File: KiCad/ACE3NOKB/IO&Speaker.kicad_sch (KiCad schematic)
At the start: 24 parts, among them Q3 BC183

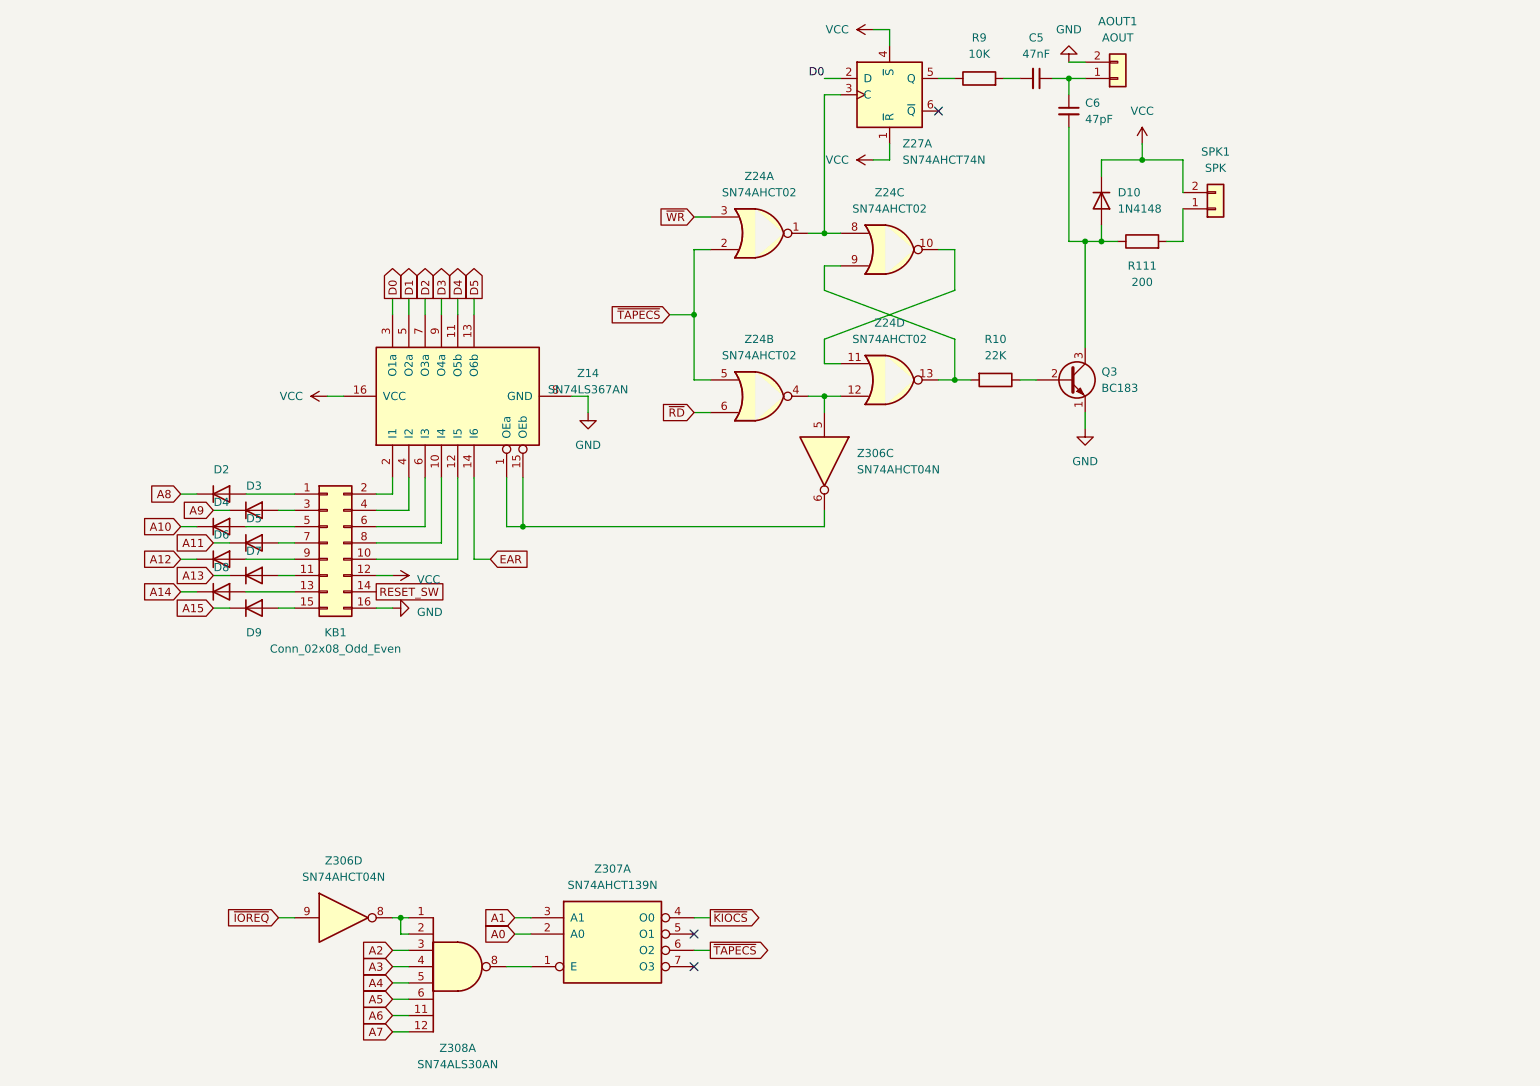
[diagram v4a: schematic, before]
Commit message: Some surface mounted devices and 1G gates for space. Switch able bwteen speeds and witha Freuqency Multiplier to augment the orginal crystal.
Signed-off-by: John Bradley <flypie@rocketmail.com>
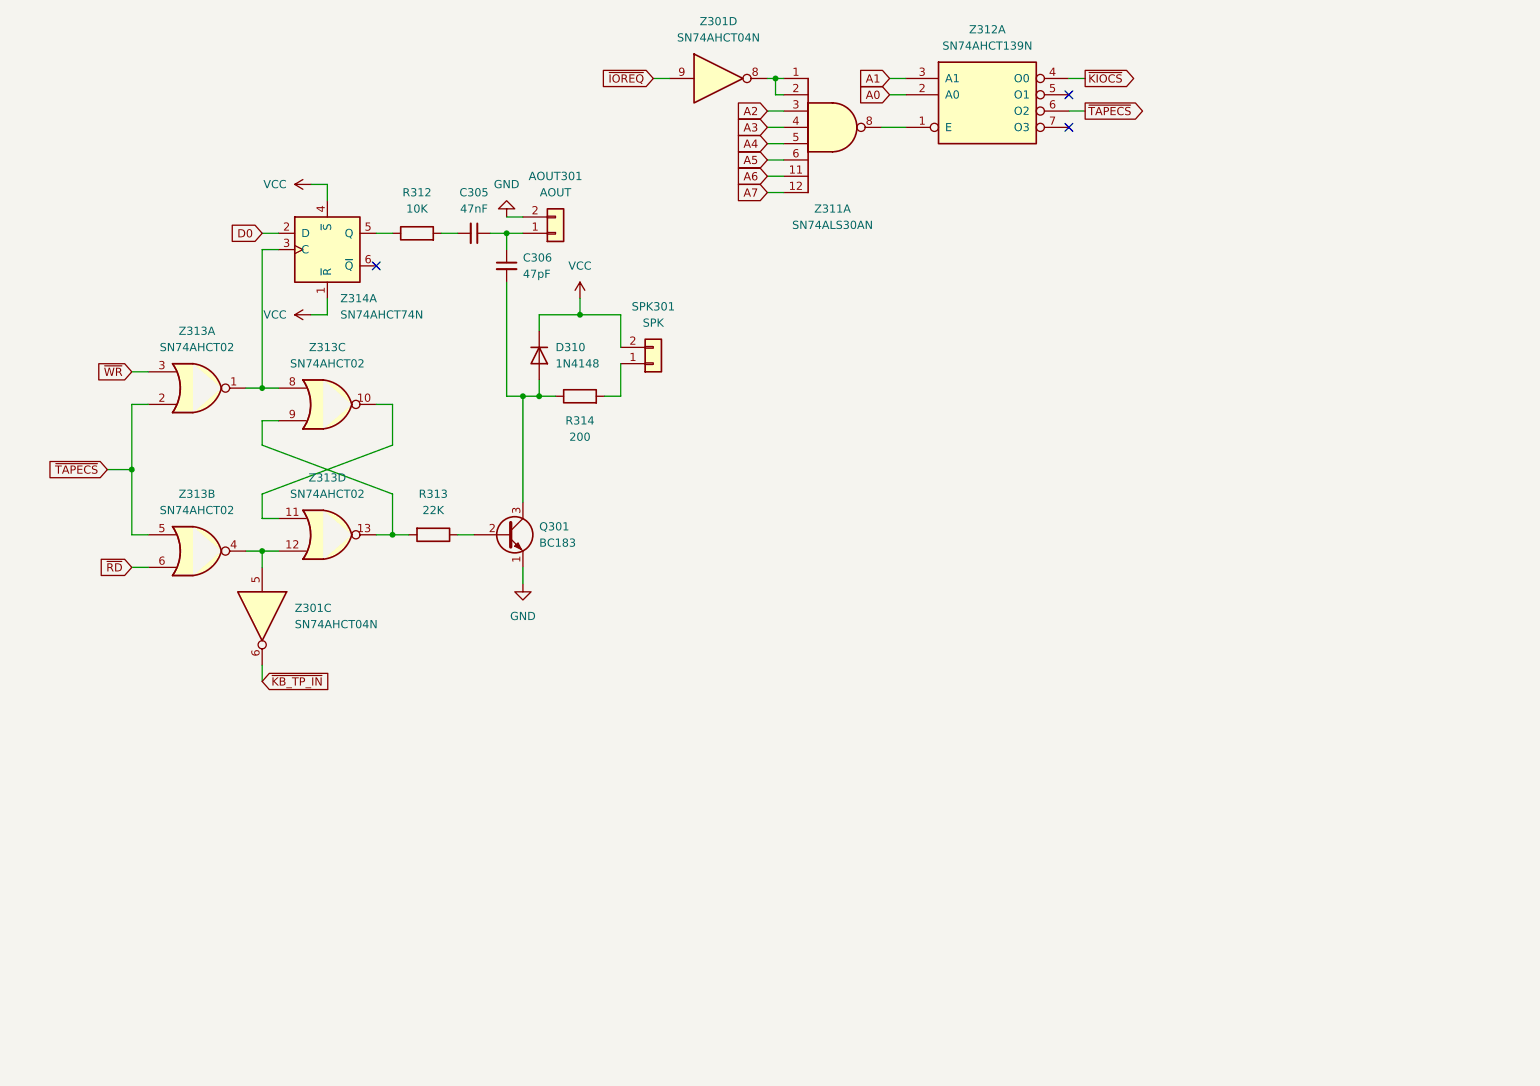
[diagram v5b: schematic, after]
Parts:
- removed D2, D3, D4, D5, D6, D7, D8, D9: 1N4148, Diode_THT:D_DO-35_SOD27_P2.54mm_Vertical_AnodeUp, symbol Diode:1N4148
- removed KB1: Conn_02x08_Odd_Even, Connector_IDC:IDC-Header_2x08_P2.54mm_Vertical, symbol Connector_Generic:Conn_02x08_Odd_Even
- removed Z14: SN74LS367AN, Package_DIP:DIP-16_W7.62mm, symbol 74xx:74LS367
- renumbered AOUT1 to AOUT301, C5 to C305, C6 to C306, D10 to D310, Q3 to Q301, R9 to R312, R10 to R313, R111 to R314, SPK1 to SPK301, Z306 to Z301, Z308 to Z311, Z307 to Z312, Z24 to Z313, Z27 to Z314
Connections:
- net ~{KB_TP_IN}: now reaches Z301.6
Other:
- moved on the sheet: AOUT301, C305, C306, D310, Q301, R312, R313, R314, SPK301, Z301C, Z301D, Z311A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

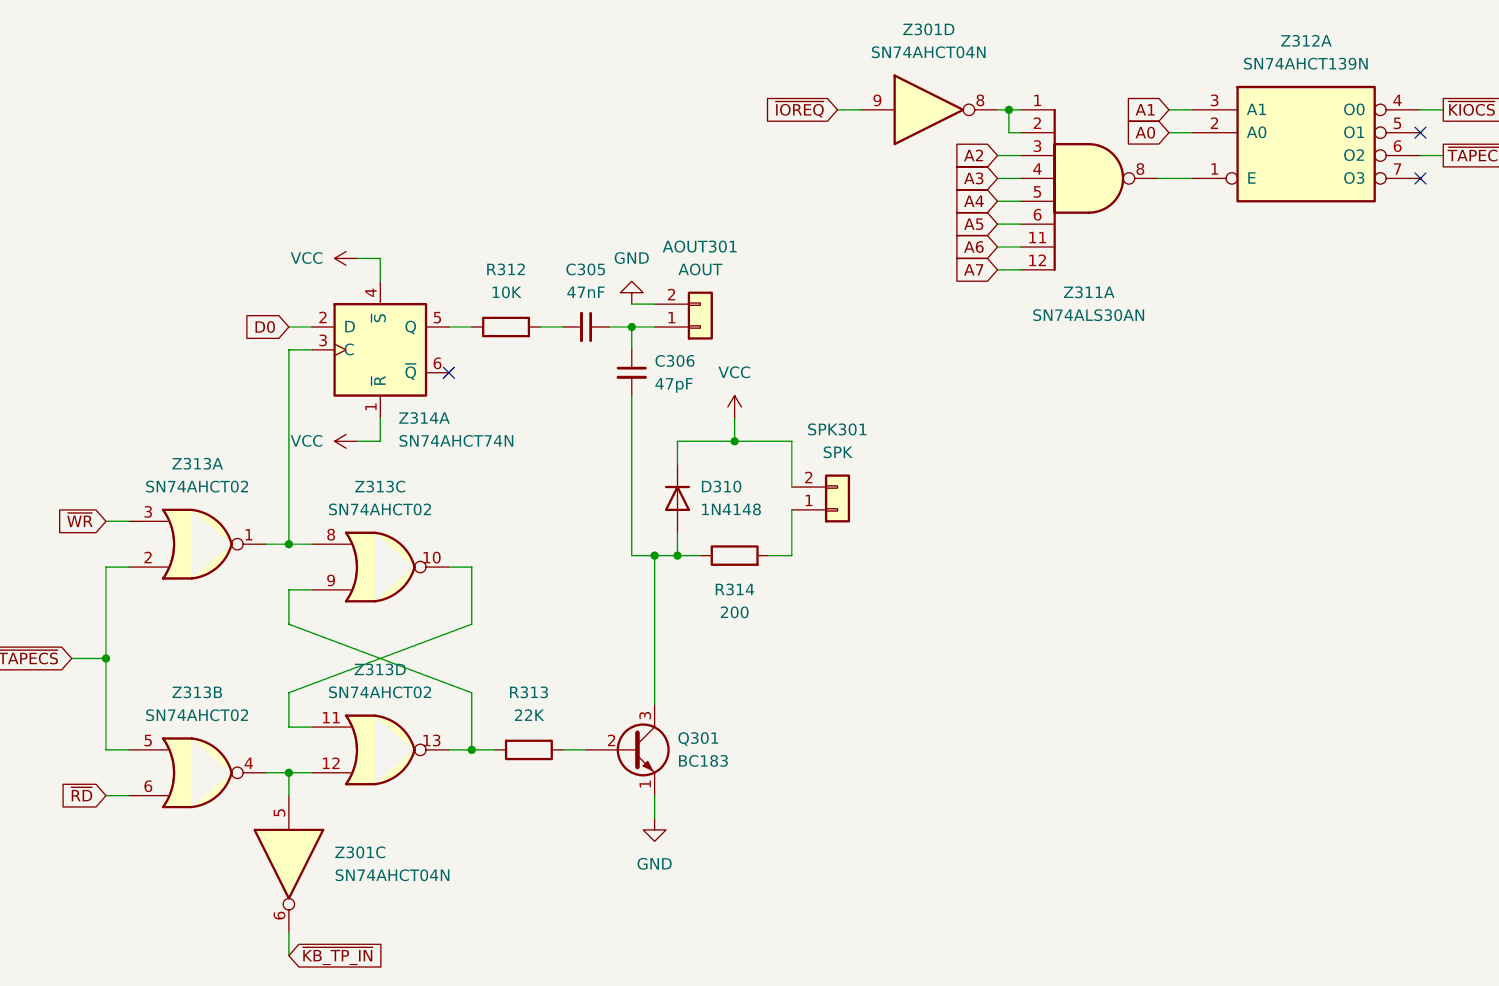
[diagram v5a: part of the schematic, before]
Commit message: Update, with new Clock Multiplier and Wait functionality.
Signed-off-by: John Bradley <flypie@rocketmail.com>
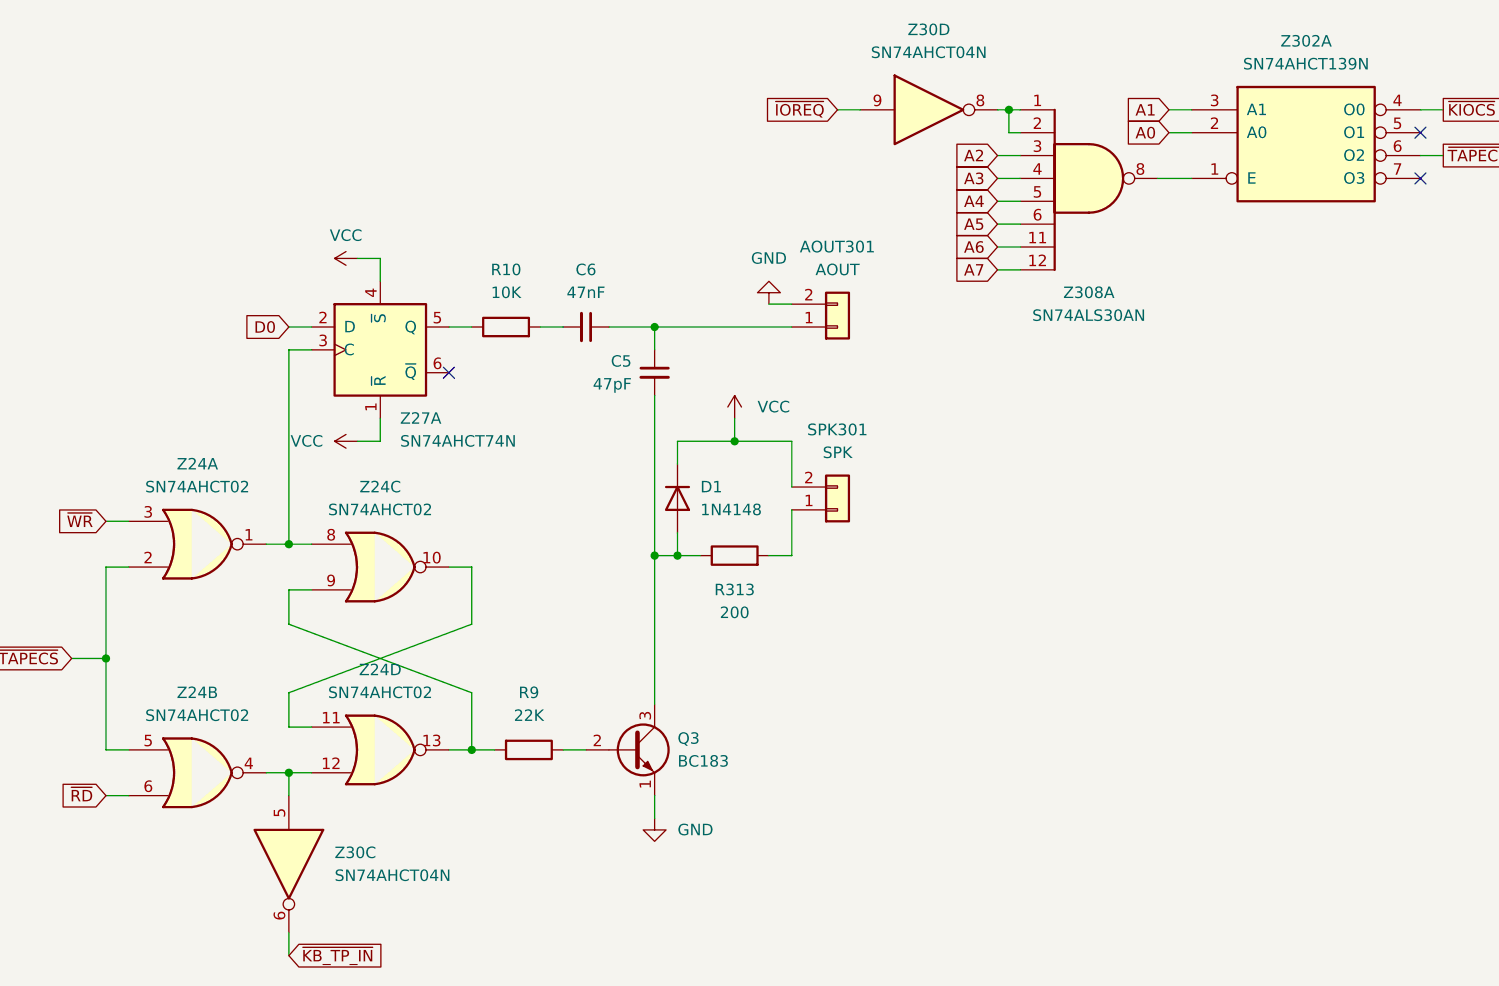
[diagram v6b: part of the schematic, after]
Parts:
- Q3: renamed from Q301; symbol Device:Q_NPN_EBC -> Transistor_BJT:Q_NPN_EBC
- R10: renamed from R312; footprint Resistor_THT:R_Axial_DIN0204_L3.6mm_D1.6mm_P1.90mm_Vertical -> Resistor_THT:R_Axial_DIN0204_L3.6mm_D1.6mm_P2.54mm_Vertical
- R313: renamed from R314; footprint Resistor_THT:R_Axial_DIN0204_L3.6mm_D1.6mm_P1.90mm_Vertical -> Resistor_THT:R_Axial_DIN0204_L3.6mm_D1.6mm_P2.54mm_Vertical
- R9: renamed from R313; footprint Resistor_THT:R_Axial_DIN0204_L3.6mm_D1.6mm_P1.90mm_Vertical -> Resistor_THT:R_Axial_DIN0204_L3.6mm_D1.6mm_P2.54mm_Vertical
- Z24: renamed from Z313; symbol 74xx:74LS02 -> 74xx-FIX:74LS02
- Z302: renamed from Z312; value SN74AHCT139N -> SN74AHCT139N
- Z308: renamed from Z311; value SN74ALS30AN -> SN74ALS30AN
- renumbered C306 to C5, C305 to C6, D310 to D1, Z314 to Z27, Z301 to Z30
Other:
- moved on the sheet: AOUT301, C5

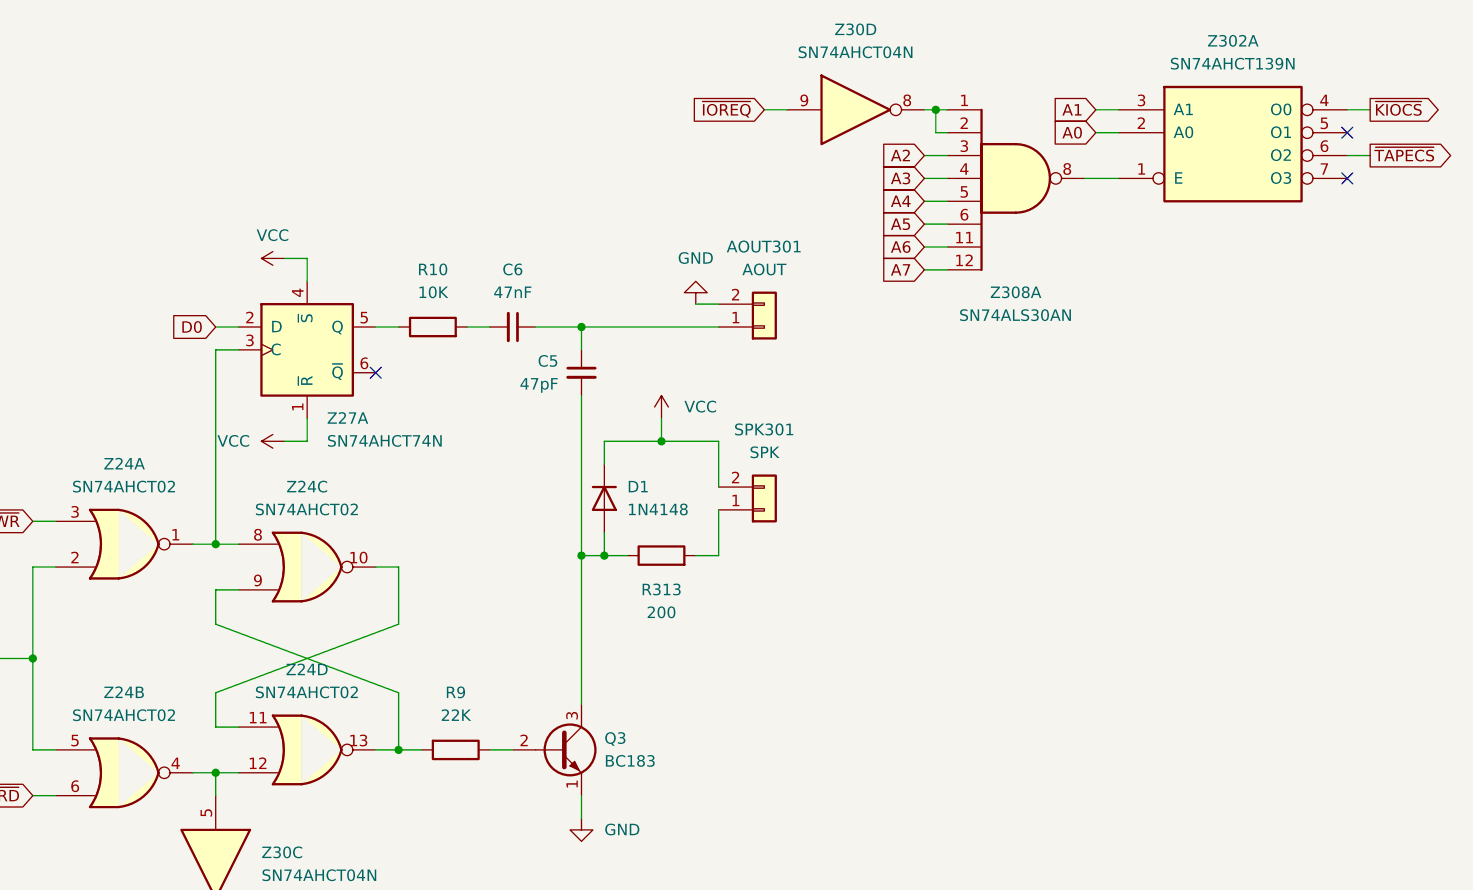
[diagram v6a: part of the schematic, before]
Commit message: Change Address decode to speed up the use of /WAIT to avoid conflicts when setting up character RAM. Rerange priority on Internal external /WAIT. Reconnect Clock to rest of circuit.
Signed-off-by: John Bradley <flypie@rocketmail.com>
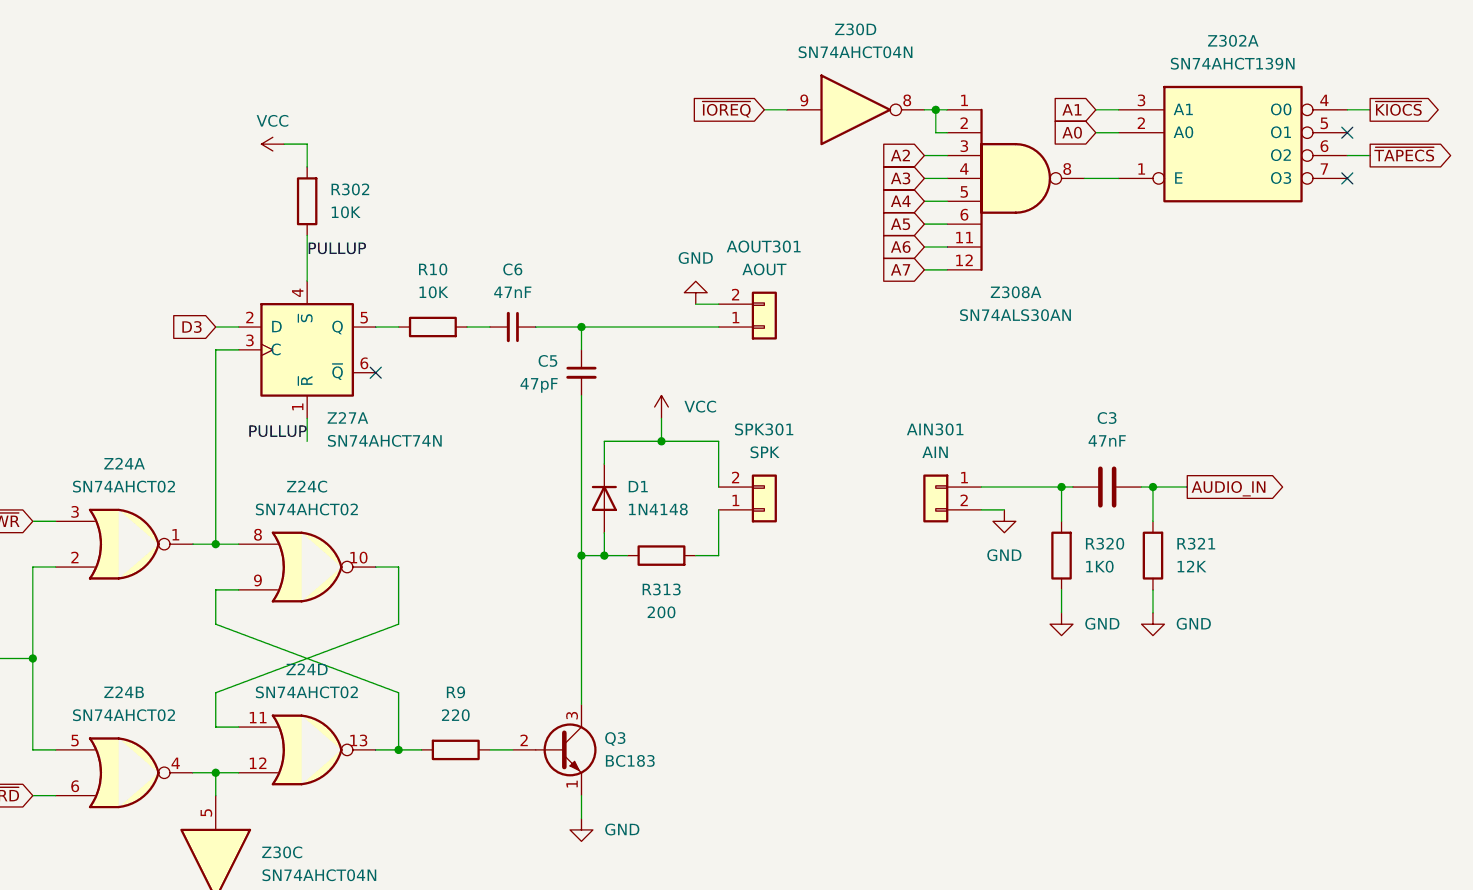
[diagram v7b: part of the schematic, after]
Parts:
- added AIN301: AIN, Connector_PinHeader_2.54mm:PinHeader_1x02_P2.54mm_Vertical, symbol Connector_Generic:Conn_01x02
- added C3: 47nF, Capacitor_THT:C_Disc_D5.0mm_W2.5mm_P2.50mm, symbol Device:C
- added R302: 10K, Resistor_THT:R_Axial_DIN0204_L3.6mm_D1.6mm_P2.54mm_Vertical, symbol Device:R
- added R320: 1K0, Resistor_THT:R_Axial_DIN0204_L3.6mm_D1.6mm_P2.54mm_Vertical, symbol Device:R
- added R321: 12K, Resistor_THT:R_Axial_DIN0204_L3.6mm_D1.6mm_P2.54mm_Vertical, symbol Device:R
- R9: value 22K -> 220
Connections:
- net GND: now also AIN301.2 (Pin_2), R320.1, R321.1
- net VCC: now also R302.2; no longer Z27.1 (~{R}), Z27.4 (~{S})
- net D0 renamed D3
- new net: AIN301.1 (Pin_1), C3.1, R320.2
- new net AUDIO_IN: C3.2, R321.2
- new net PULLUP: R302.1, Z27.1 (~{R}), Z27.4 (~{S})
